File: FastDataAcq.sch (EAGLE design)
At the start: 224 parts, among them IC1 LT1963AEQ, IC2 FT230XQ, IC3 ADCMP553BRMZ, J1 MICRO-FIT_3.0_2POS_RA_SMD, J2 USB_MICROAB_SMT, J3 HEADER_0.1"_10P_2R_SMT, X1 87832-14, X2 SMA-142-0701-801/806, X3 SMA-142-0701-801/806, Y1 SI530-500, Y2 100MHz, Y3 DNP

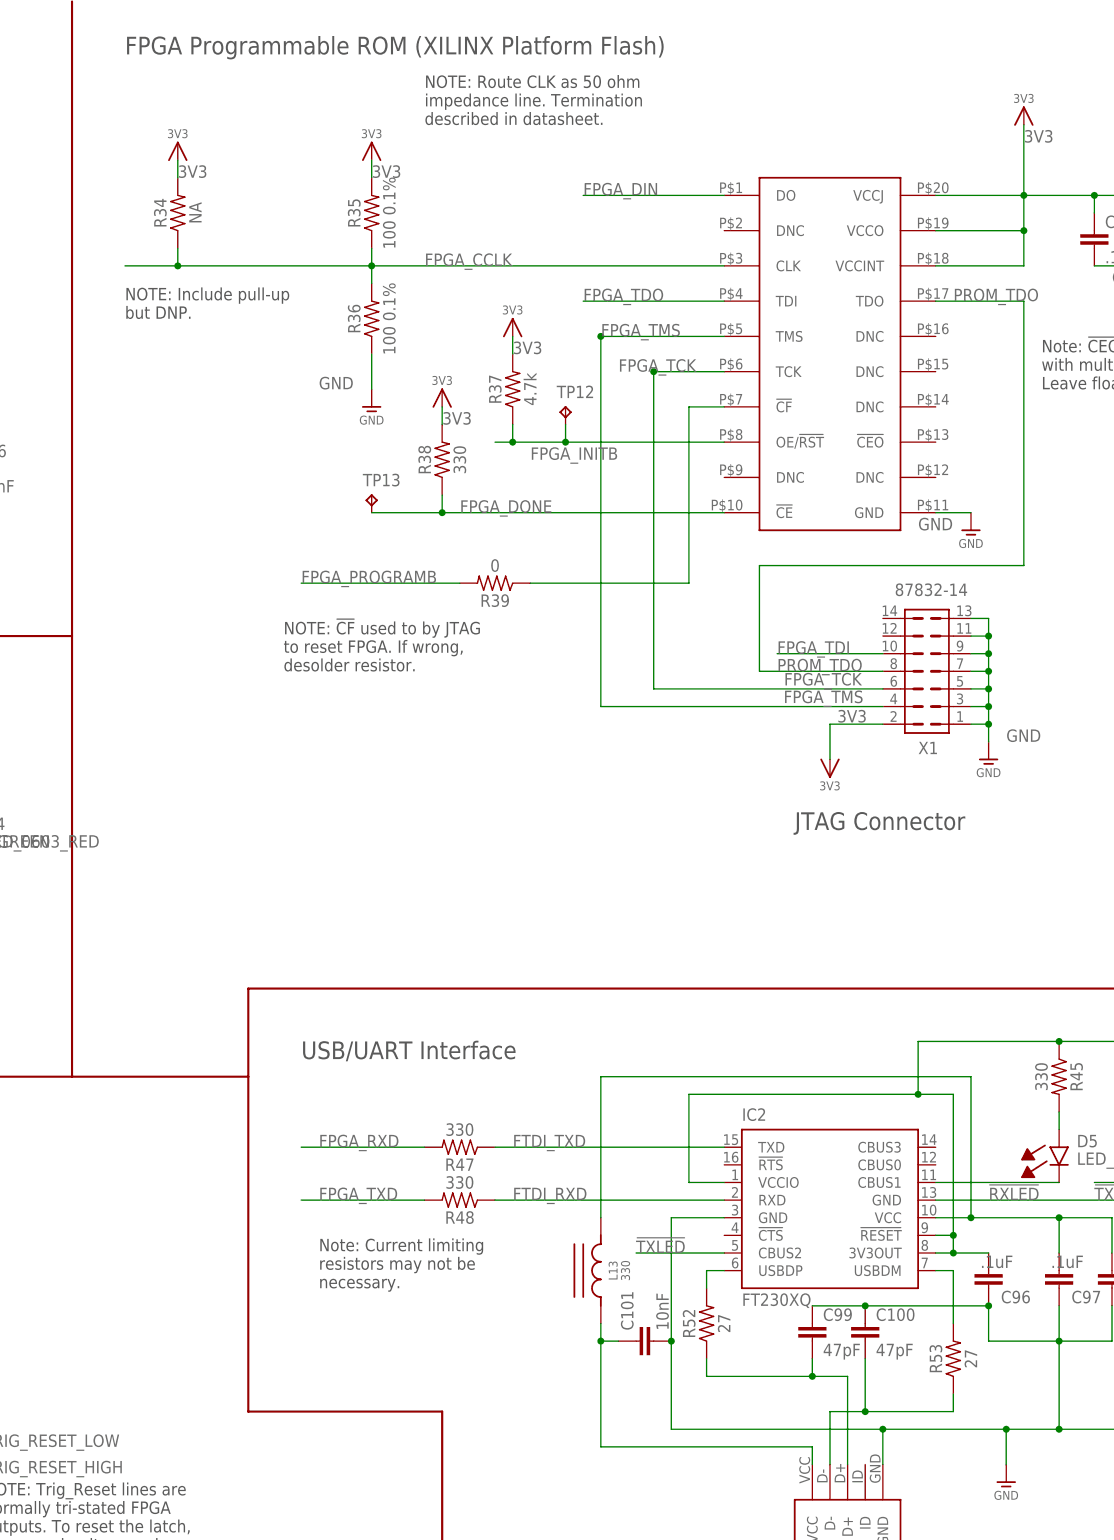
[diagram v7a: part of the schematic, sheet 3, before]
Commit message: Digital routing almost done.
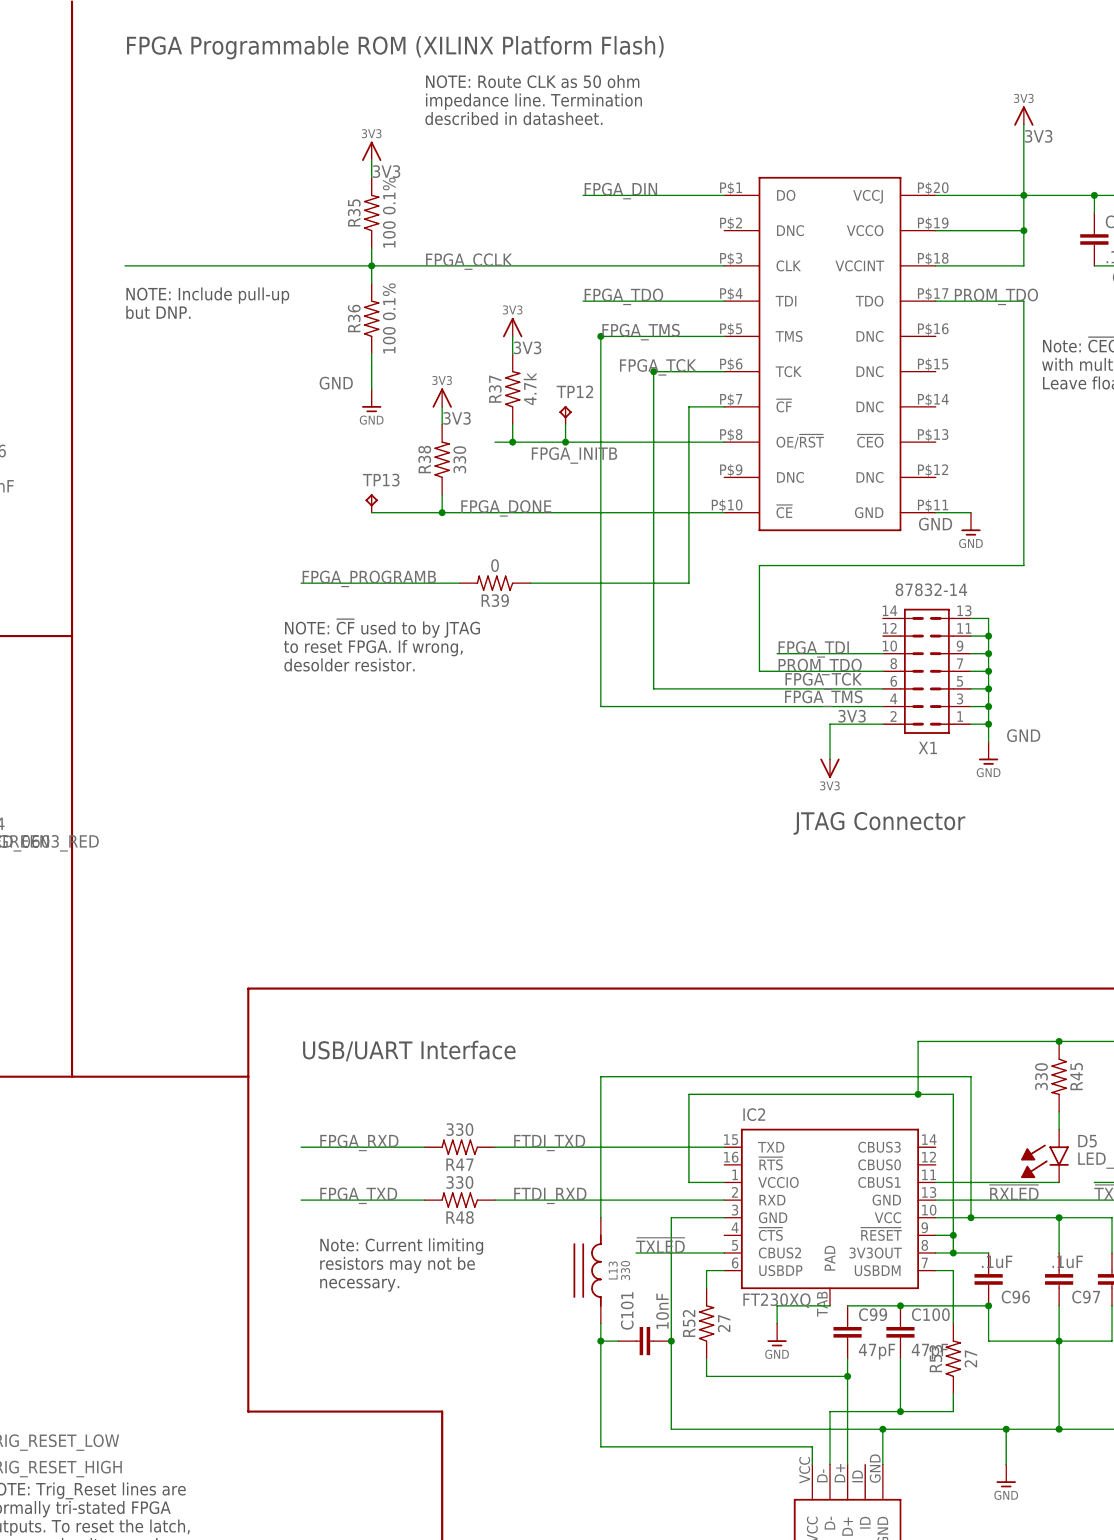
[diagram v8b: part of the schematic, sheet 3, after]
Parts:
- removed R34: NA, rcl:R-US_R0603
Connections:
- new net N3: U$2.IO_L12P_D1_MISO2_2
- new net N4: U$2.IO_L12N_D2_MISO3_2
- new net N5: U$2.IO_L13N_D10_2
- new net N6: U$2.IO_L14P_D11_2
- new net N7: U$2.IO_L14N_D12_2
- new net N8: U$2.IO_L48P_D7_2
- new net N9: U$2.IO_L48N_RDWR_B_VREF_2
- net 3V3: no longer R34.2
- net ADC_PWR_EN: now also U$2.IO_L64P_D8_2; no longer U$2.IO_L48P_D7_2
- net ANALOG_PWR_EN: now also U$2.IO_L64N_D9_2; no longer U$2.IO_L48N_RDWR_B_VREF_2
- net FPGA_CCLK: no longer R34.1
- net FPGA_GPIO1: no longer U$2.IO_L14N_D12_2
- net FPGA_GPIO2: no longer U$2.IO_L14P_D11_2
- net FPGA_GPIO3: no longer U$2.IO_L13N_D10_2
- net FPGA_GPIO4: no longer U$2.IO_L12N_D2_MISO3_2
- net FPGA_GPIO5: no longer U$2.IO_L12P_D1_MISO2_2
- net FPGA_GPIO6: no longer U$2.IO_L3N_MOSI_CSI_B_MISO0_2
- net FPGA_GPIO7: no longer U$2.IO_L2P_CMPCLK_2
- net FPGA_RXD: now also U$2.IO_L2P_CMPCLK_2; no longer U$2.IO_L64P_D8_2
- net FPGA_TXD: now also U$2.IO_L3N_MOSI_CSI_B_MISO0_2; no longer U$2.IO_L64N_D9_2
- net GND: now also IC2.PAD
- net TRIG_RESET_HIGH: now also U$2.IO_L49N_D4_2; no longer U$2.IO_L49P_D3_2
- net TRIG_RESET_LOW: now also U$2.IO_L49P_D3_2; no longer U$2.IO_L49N_D4_2
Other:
- moved on the sheet: C100, C99
